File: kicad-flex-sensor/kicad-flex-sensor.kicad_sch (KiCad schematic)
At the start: 6 parts, among them J1 Power, J2 Digital/PWM, J3 Analog, J4 Digital/PWM

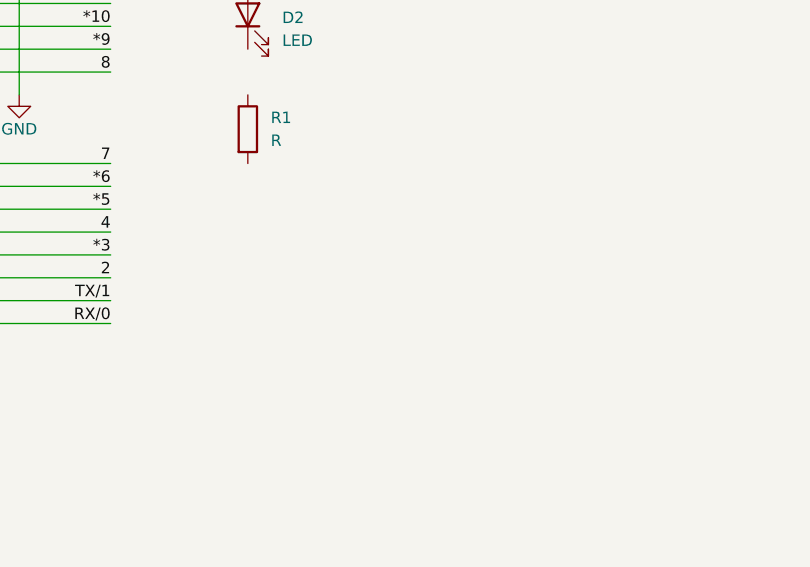
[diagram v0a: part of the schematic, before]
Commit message: add bluetooth symbol and footprint
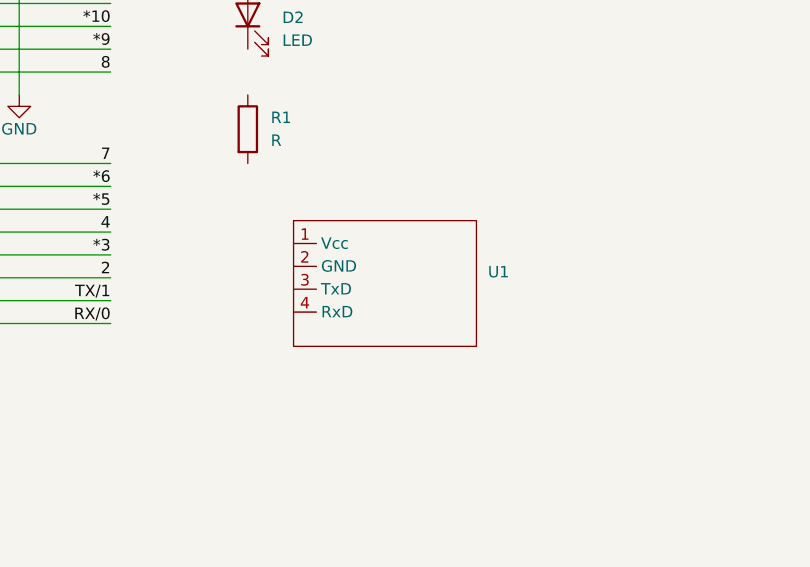
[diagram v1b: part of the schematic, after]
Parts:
- added U1: ~, graphite_empreinte:Bluetooth_empreinte, symbol Graphite_symbol:Bluetooth
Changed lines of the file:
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@@
+	)
+	(symbol
+		(lib_id "Graphite_symbol:Bluetooth")
+		(at 105.41 72.39 0)
+		(unit 1)
+		(exclude_from_sim no)
+		(in_bom yes)
+		(on_board yes)
+		(dnp no)
+		(fields_autoplaced yes)
+		(property "Reference" "U1"
+			(at 116.84 71.7549 0)
+			(effects
+				(font
+					(size 1.27 1.27)
+				)
+				(justify left)
+			)
+		)
+		(property "Value" "~"
+			(at 116.84 74.2949 0)
+			(effects
+				(font
+					(size 1.27 1.27)
+				)
+				(justify left)
+			)
+		)
+		(property "Footprint" "graphite_empreinte:Bluetooth_empreinte"
+			(at 105.41 72.39 0)
+			(effects
+				(font
+					(size 1.27 1.27)
+				)
+				(hide yes)
+			)
+		)
+		(property "Datasheet" ""
+			(at 105.41 72.39 0)
+			(effects
+				(font
+					(size 1.27 1.27)
+				)
+				(hide yes)
+			)
+		)
+		(property "Description" ""
+			(at 105.41 72.39 0)
+			(effects
+				(font
+					(size 1.27 1.27)
+				)
+				(hide yes)
+			)
+		)
+		(pin "2"
+		)
+		(pin "1"
+		)
+		(pin "4"
+		)
+		(pin "3"
+		)
+		(instances
+			(project ""
+				(path "/e63e39d7-6ac0-4ffd-8aa3-1841a4541b55"
+					(reference "U1")
+					(unit 1)
+				)
+			)
+		)
 	)
 	(symbol

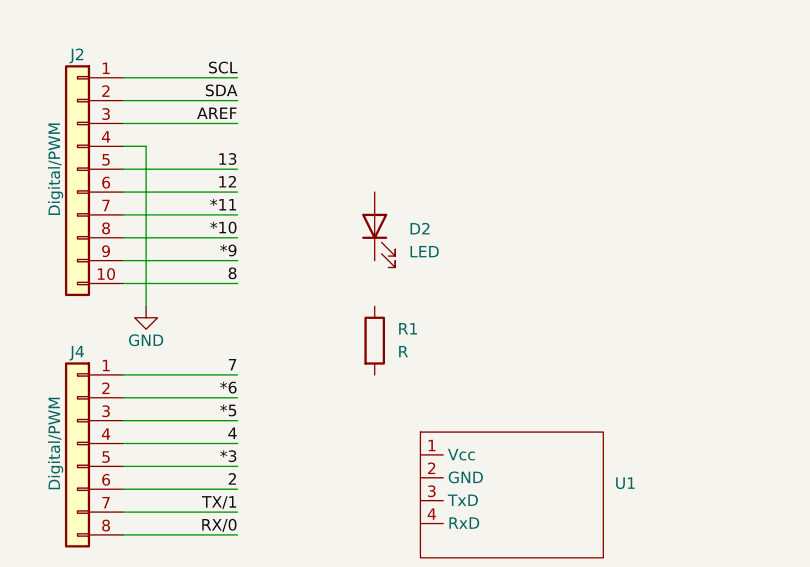
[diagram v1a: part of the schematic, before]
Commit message: rm res and cap
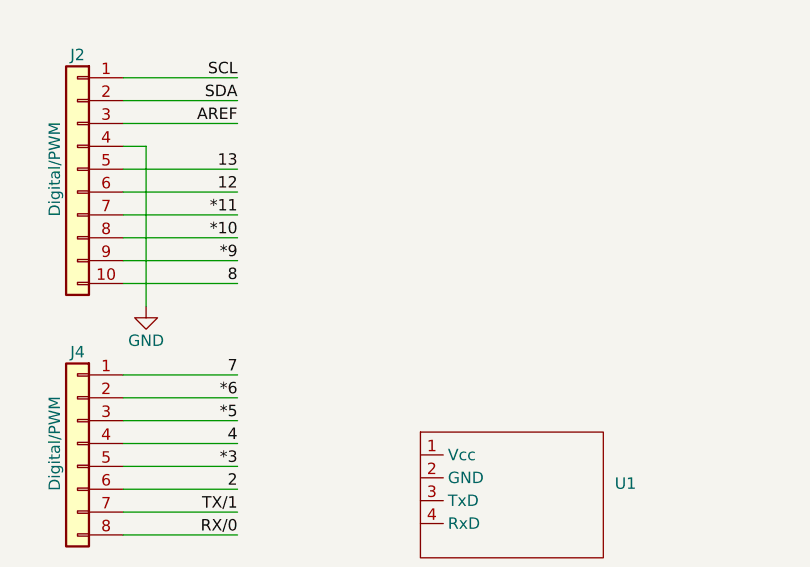
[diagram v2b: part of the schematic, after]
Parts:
- removed D2: LED, symbol Device:LED
- removed R1: R, symbol Device:R
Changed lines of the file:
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@@
-	)
-	(symbol
-		(lib_id "Device:LED")
-		(at 90.17 43.18 90)
-		(unit 1)
-		(exclude_from_sim no)
-		(in_bom yes)
-		(on_board yes)
-		(dnp no)
-		(fields_autoplaced yes)
-		(property "Reference" "D2"
-			(at 93.98 43.4974 90)
-			(effects
-				(font
-					(size 1.27 1.27)
-				)
-				(justify right)
-			)
-		)
-		(property "Value" "LED"
-			(at 93.98 46.0374 90)
-			(effects
-				(font
-					(size 1.27 1.27)
-				)
-				(justify right)
-			)
-		)
-		(property "Footprint" ""
-			(at 90.17 43.18 0)
-			(effects
-				(font
-					(size 1.27 1.27)
-				)
-				(hide yes)
-			)
-		)
-		(property "Datasheet" "~"
-			(at 90.17 43.18 0)
-			(effects
-				(font
-					(size 1.27 1.27)
-				)
-				(hide yes)
-			)
-		)
-		(property "Description" "Light emitting diode"
-			(at 90.17 43.18 0)
-			(effects
-				(font
-					(size 1.27 1.27)
-				)
-				(hide yes)
-			)
-		)
-		(property "Sim.Pins" "1=K 2=A"
-			(at 90.17 43.18 0)
-			(effects
-				(font
-					(size 1.27 1.27)
-				)
-				(hide yes)
-			)
-		)
-		(pin "2"
-		)
-		(pin "1"
-		)
-		(instances
-			(project ""
-				(path "/e63e39d7-6ac0-4ffd-8aa3-1841a4541b55"
-					(reference "D2")
-					(unit 1)
-				)
-			)
-		)
 	)
 	(symbol
@@
 					(unit 1)
 				)
-			)
-		)
-	)
-	(symbol
-		(lib_id "Device:R")
-		(at 90.17 55.88 0)
-		(unit 1)
-		(exclude_from_sim no)
-		(in_bom yes)
-		(on_board yes)
-		(dnp no)
-		(fields_autoplaced yes)
-		(property "Reference" "R1"
-			(at 92.71 54.6099 0)
-			(effects
-				(font
-					(size 1.27 1.27)
-				)
-				(justify left)
-			)
-		)
-		(property "Value" "R"
-			(at 92.71 57.1499 0)
-			(effects
-				(font
-					(size 1.27 1.27)
-				)
-				(justify left)
-			)
-		)
-		(property "Footprint" ""
-			(at 88.392 55.88 90)
-			(effects
-				(font
-					(size 1.27 1.27)
-				)
-				(hide yes)
-			)
-		)
-		(property "Datasheet" "~"
-			(at 90.17 55.88 0)
-			(effects
-				(font
-					(size 1.27 1.27)
-				)
-				(hide yes)
-			)
-		)
-		(property "Description" "Resistor"
-			(at 90.17 55.88 0)
-			(effects
-				(font
-					(size 1.27 1.27)
-				)
-				(hide yes)
-			)
-		)
-		(pin "2"
-		)
-		(pin "1"
-		)
-		(instances
-			(project ""
-				(path "/e63e39d7-6ac0-4ffd-8aa3-1841a4541b55"
-					(reference "R1")
-					(unit 1)
-				)

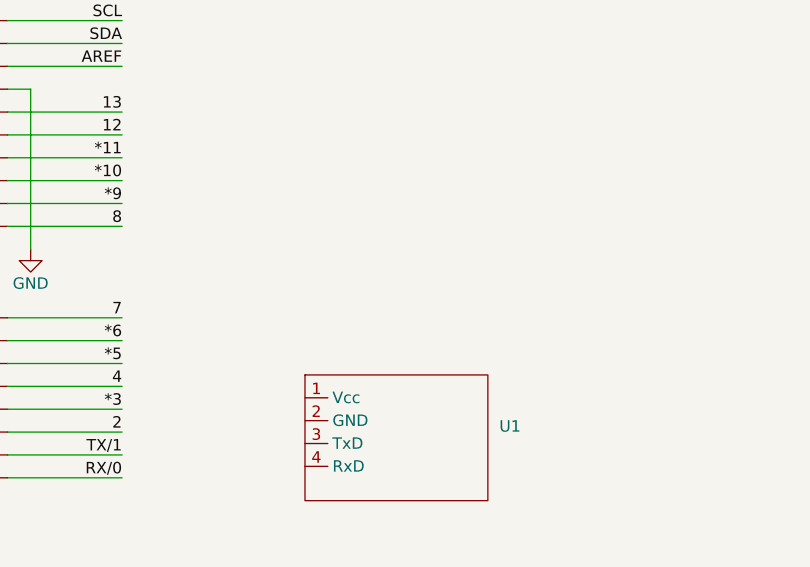
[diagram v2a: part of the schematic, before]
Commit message: add schema OLED
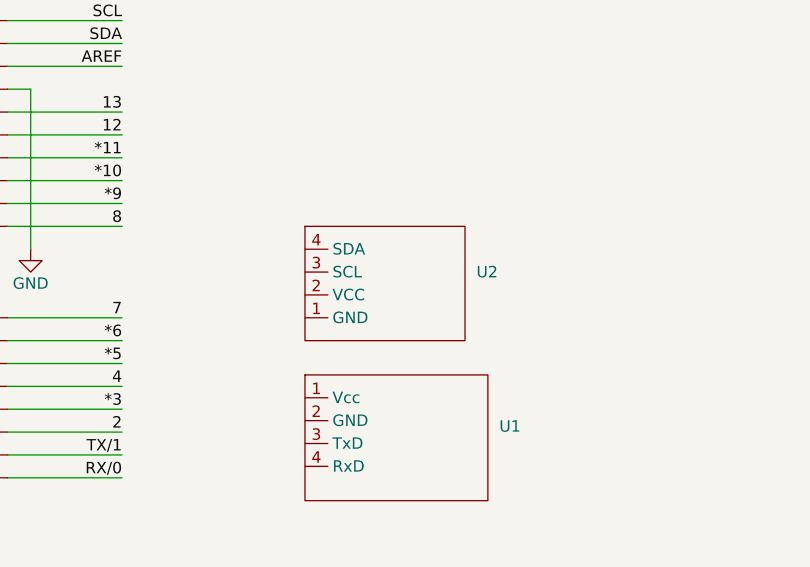
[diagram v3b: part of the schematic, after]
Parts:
- added U2: ~, symbol Graphite_symbol:OLED
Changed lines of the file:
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@@
+		)
+	)
+	(symbol
+		(lib_id "Graphite_symbol:OLED")
+		(at 104.14 55.88 0)
+		(unit 1)
+		(exclude_from_sim no)
+		(in_bom yes)
+		(on_board yes)
+		(dnp no)
+		(fields_autoplaced yes)
+		(property "Reference" "U2"
+			(at 114.3 54.6099 0)
+			(effects
+				(font
+					(size 1.27 1.27)
+				)
+				(justify left)
+			)
+		)
+		(property "Value" "~"
+			(at 114.3 57.1499 0)
+			(effects
+				(font
+					(size 1.27 1.27)
+				)
+				(justify left)
+			)
+		)
+		(property "Footprint" ""
+			(at 104.14 55.88 0)
+			(effects
+				(font
+					(size 1.27 1.27)
+				)
+				(hide yes)
+			)
+		)
+		(property "Datasheet" ""
+			(at 104.14 55.88 0)
+			(effects
+				(font
+					(size 1.27 1.27)
+				)
+				(hide yes)
+			)
+		)
+		(property "Description" ""
+			(at 104.14 55.88 0)
+			(effects
+				(font
+					(size 1.27 1.27)
+				)
+				(hide yes)
+			)
+		)
+		(pin "3"
+		)
+		(pin "1"
+		)
+		(pin "2"
+		)
+		(pin "4"
+		)
+		(instances
+			(project ""
+				(path "/e63e39d7-6ac0-4ffd-8aa3-1841a4541b55"
+					(reference "U2")
+					(unit 1)
+				)
+			)
 		)
 	)
